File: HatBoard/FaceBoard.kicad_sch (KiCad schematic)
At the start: 8 parts, among them J1 Molex FC Connection, J2 DF11 FC Connection, J3 Conn_01x04, U4 TCA4311A

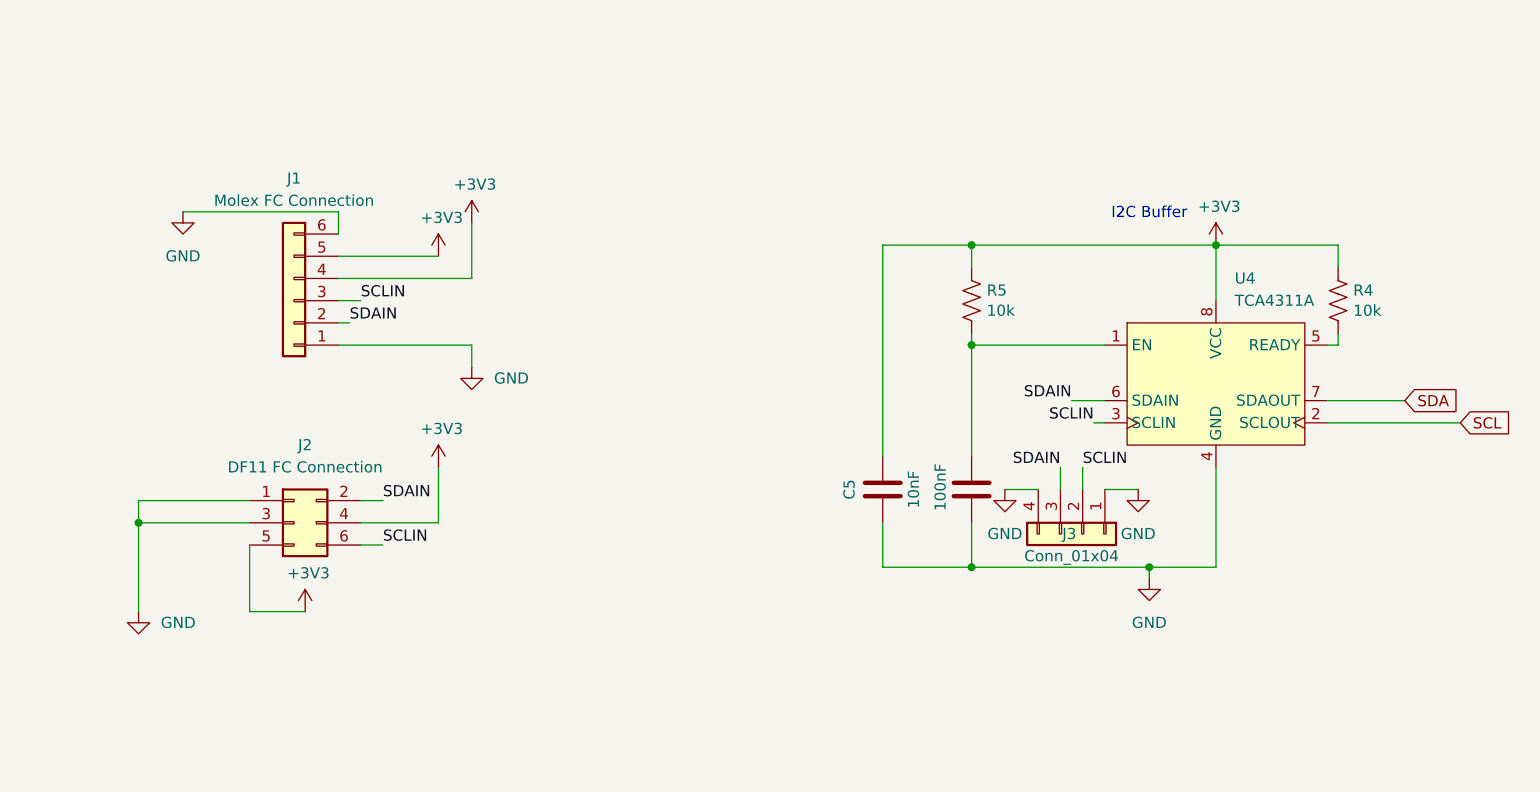
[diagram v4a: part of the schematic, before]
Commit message: added modifications for 2 cables
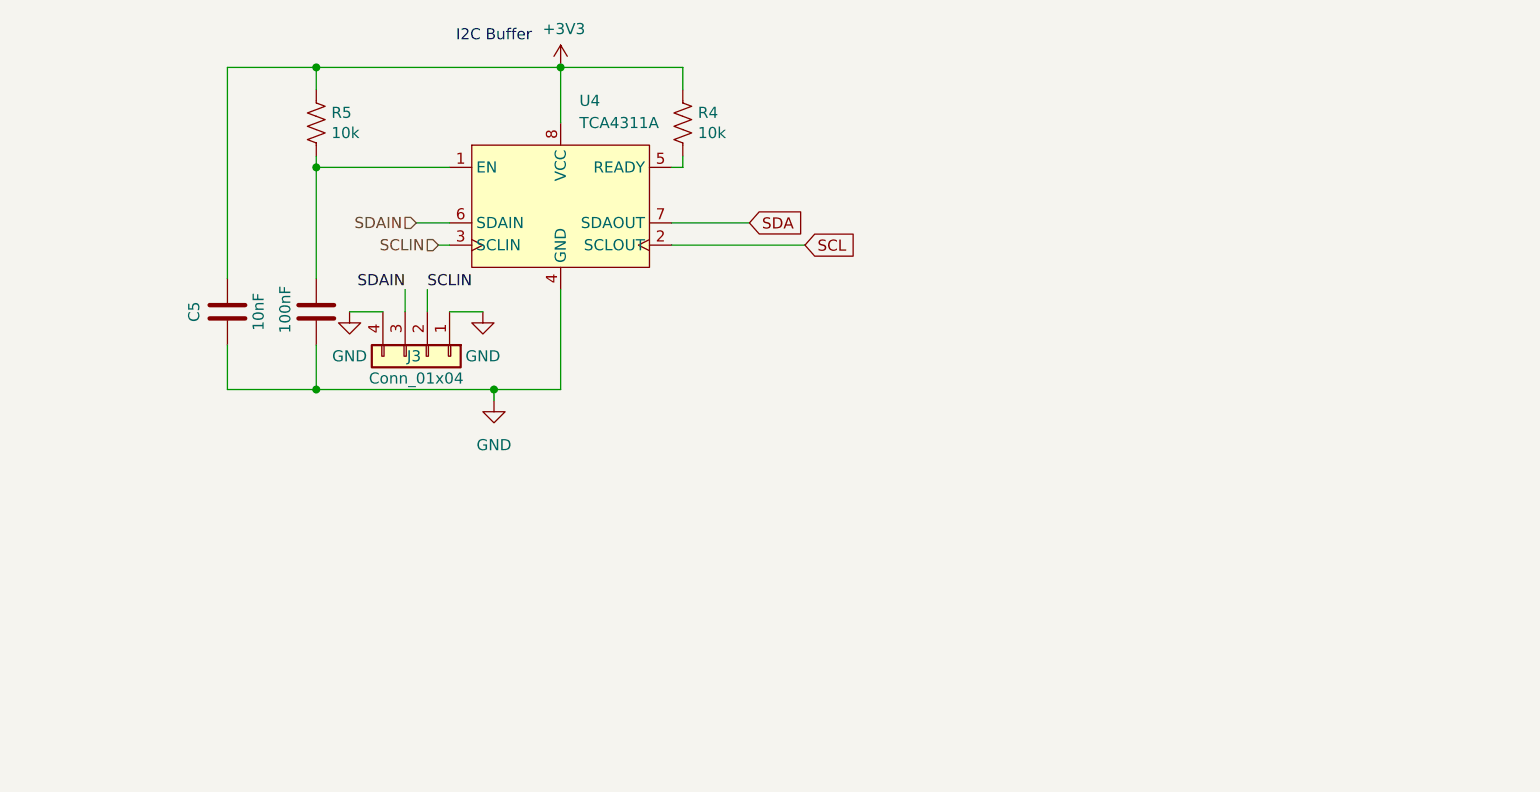
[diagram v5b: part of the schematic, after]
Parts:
- removed J1: Molex FC Connection, easyeda2kicad:CONN-SMD_6P-P1.50_A1501WRB-S-6P, symbol Connector_Generic:Conn_01x06
- removed J2: DF11 FC Connection, Connector_Hirose:Hirose_DF11-6DP-2DSA_2x03_P2.00mm_Vertical, symbol Connector_Generic:Conn_02x03_Odd_Even
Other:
- moved on the sheet: C5, J3, R4, R5, U4

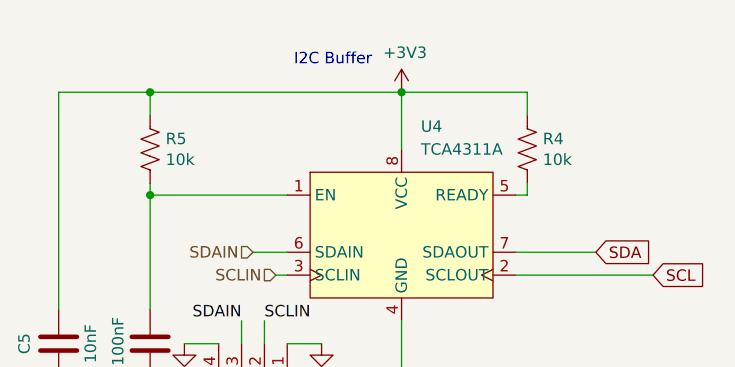
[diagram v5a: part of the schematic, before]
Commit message: placement for face baord attachment
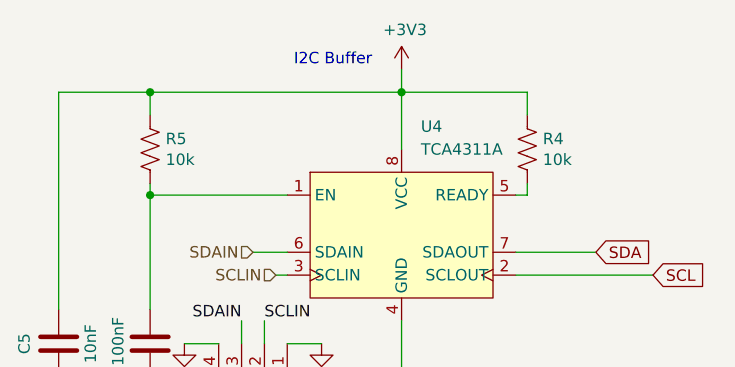
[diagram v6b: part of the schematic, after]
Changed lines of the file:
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@@
+	(wire
+		(pts
+			(xy 125.73 45.72) (xy 125.73 52.07)
+		)
+		(stroke
+			(width 0)
+			(type default)
+		)
+	)
 	(wire
 		(pts
@@
 	(wire
 		(pts
-			(xy 125.73 52.07) (xy 125.73 45.72)
+			(xy 125.73 43.18) (xy 125.73 45.72)
 		)
 		(stroke
@@
 	(symbol
 		(lib_id "solar-panel-side-Z-rescue:+3.3V-power")
-		(at 125.73 45.72 0)
+		(at 125.73 43.18 0)
 		(unit 1)
 		(exclude_from_sim no)
@@
 		(dnp no)
 		(property "Reference" "#PWR03"
-			(at 125.73 49.53 0)
+			(at 125.73 46.99 0)
 			(effects
 				(font
@@
 		)
 		(property "Value" "+3V3"
-			(at 126.111 41.3258 0)
+			(at 126.111 38.7858 0)
 			(effects
 				(font
@@
 		)
 		(property "Footprint" ""
-			(at 125.73 45.72 0)
+			(at 125.73 43.18 0)
 			(effects
 				(font
@@
 		)
 		(property "Datasheet" ""
-			(at 125.73 45.72 0)
+			(at 125.73 43.18 0)
 			(effects
 				(font
@@
 		)
 		(property "Description" ""
-			(at 125.73 45.72 0)
-			(effects
-				(font
+			(at 125.73 43.18 0)
+			(effects
+				(font

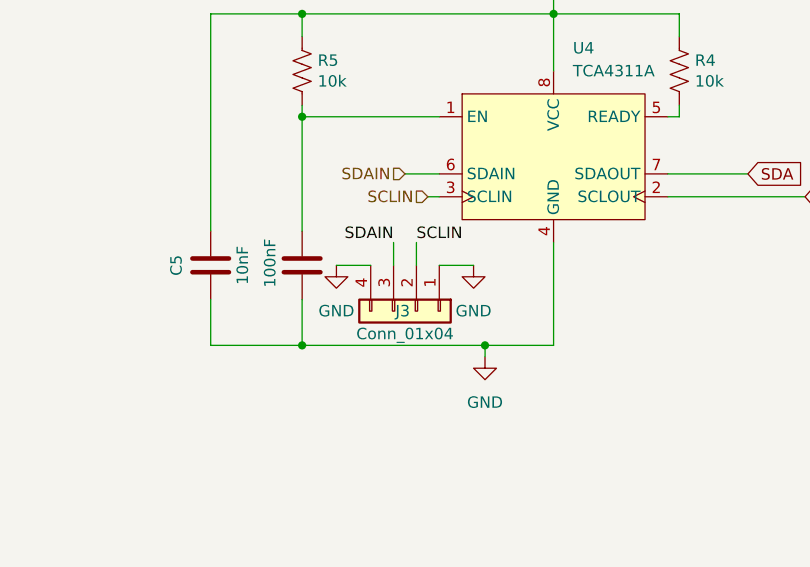
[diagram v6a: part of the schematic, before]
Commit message: corrected PCB design
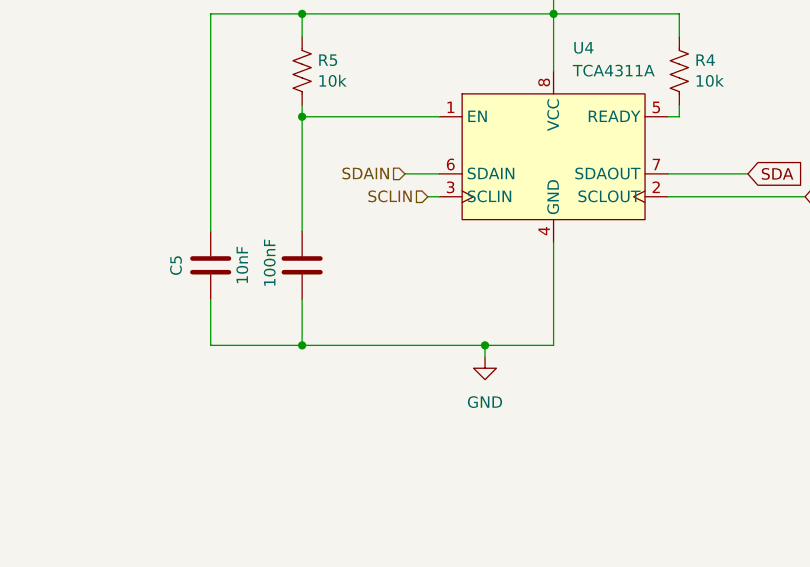
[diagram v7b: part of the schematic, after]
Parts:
- removed J3: Conn_01x04, Connector_PinHeader_2.00mm:PinHeader_1x04_P2.00mm_Vertical, symbol Connector_Generic:Conn_01x04

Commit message: diode added
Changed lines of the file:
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@@
 	(wire
 		(pts
-			(xy 138.43 66.04) (xy 153.67 66.04)
+			(xy 138.43 66.04) (xy 147.32 66.04)
 		)
 		(stroke
@@
 	(global_label "SCL"
 		(shape input)
-		(at 153.67 66.04 0)
+		(at 147.32 66.04 0)
 		(fields_autoplaced yes)
 		(effects
@@
 		)
 		(property "Intersheetrefs" "${INTERSHEET_REFS}"
-			(at 159.5086 66.04 0)
+			(at 153.1586 66.04 0)
 			(effects
 				(font
